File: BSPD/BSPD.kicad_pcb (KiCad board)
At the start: 2 copper layers, 9 parts, among them J1 350826-1, J2 440054-2, U1 LM339DR, U2 R-78E5.0-0.5, U3 SN74LVC1G3208DBVT, U4 SN74LVC3G14DCUR, U5 NE555DR, U6 SN74LVC1G08DBVR, U7 SN74AC32DR

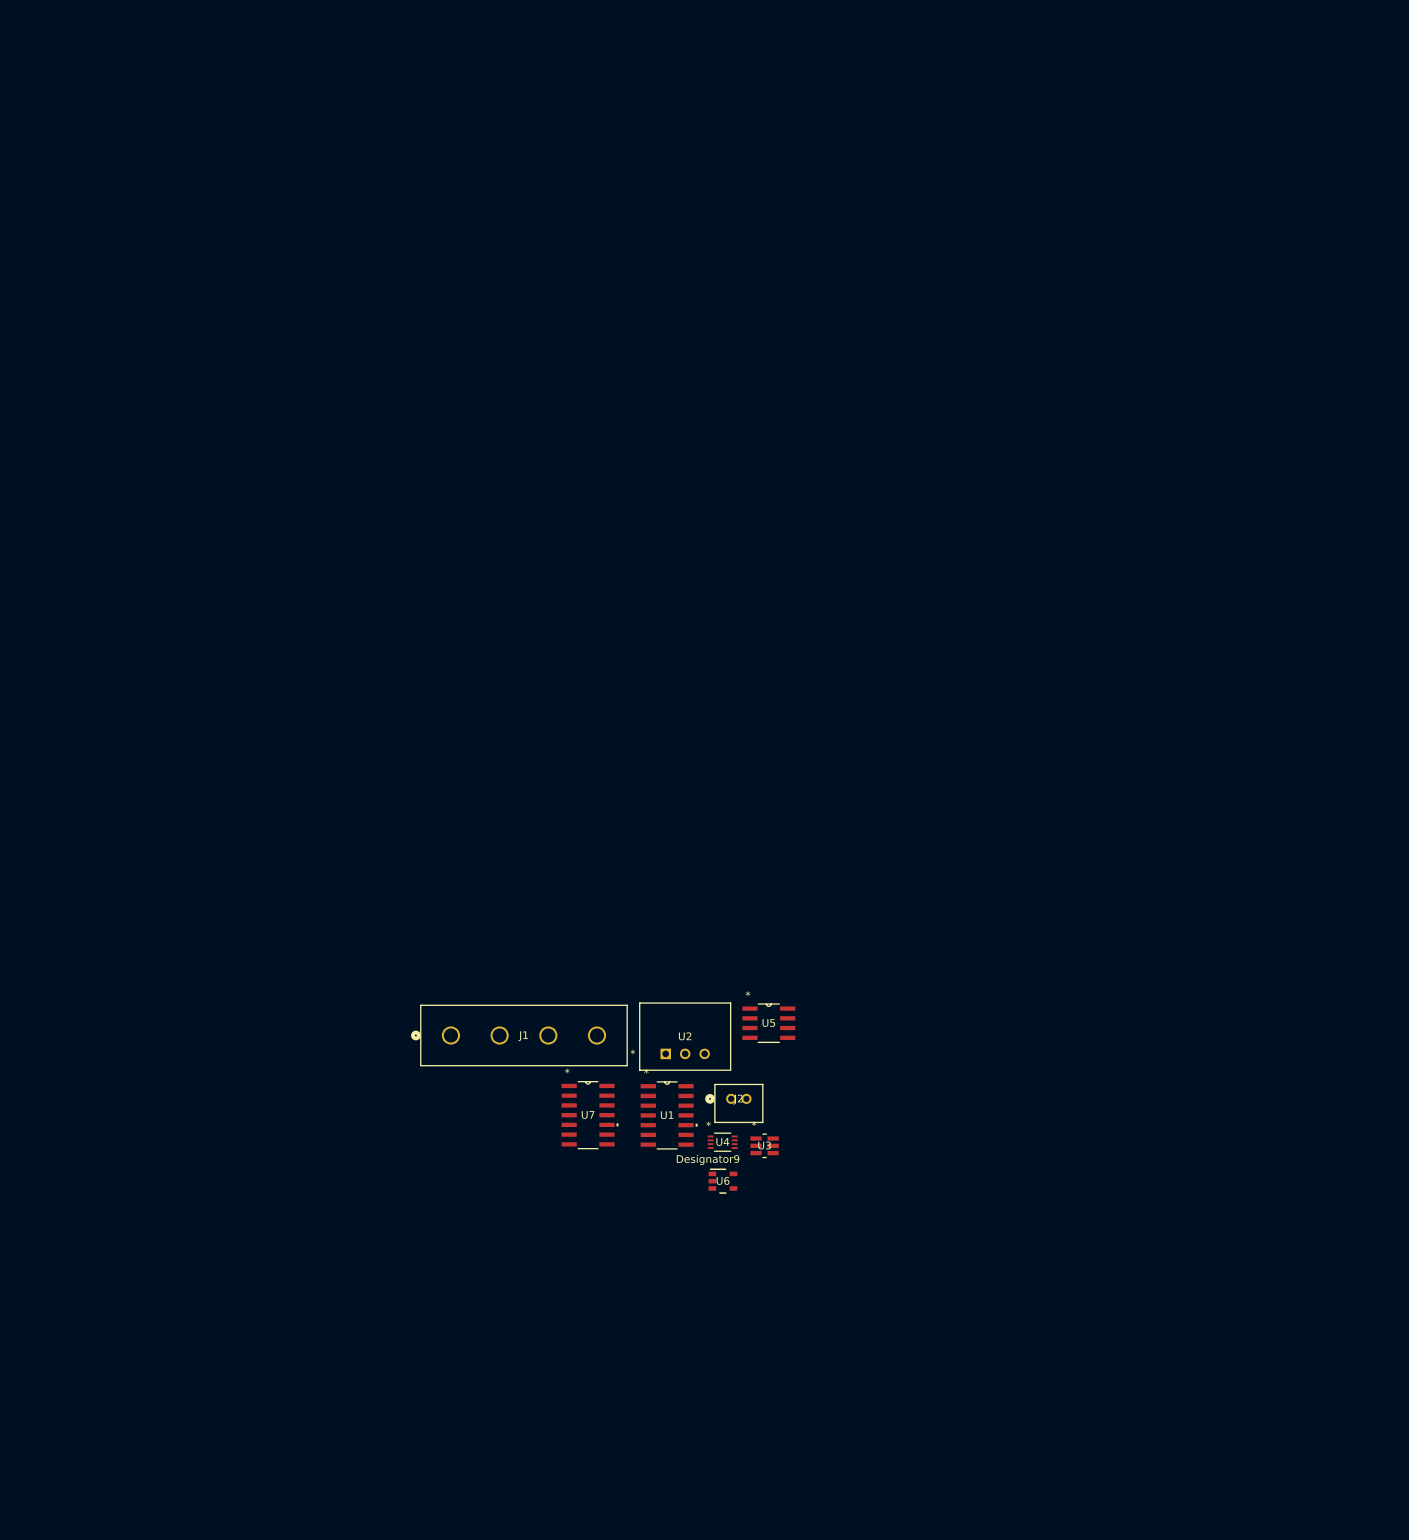
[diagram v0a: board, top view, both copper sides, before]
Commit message: Added footprints,implemented changes from meeting, starting layout
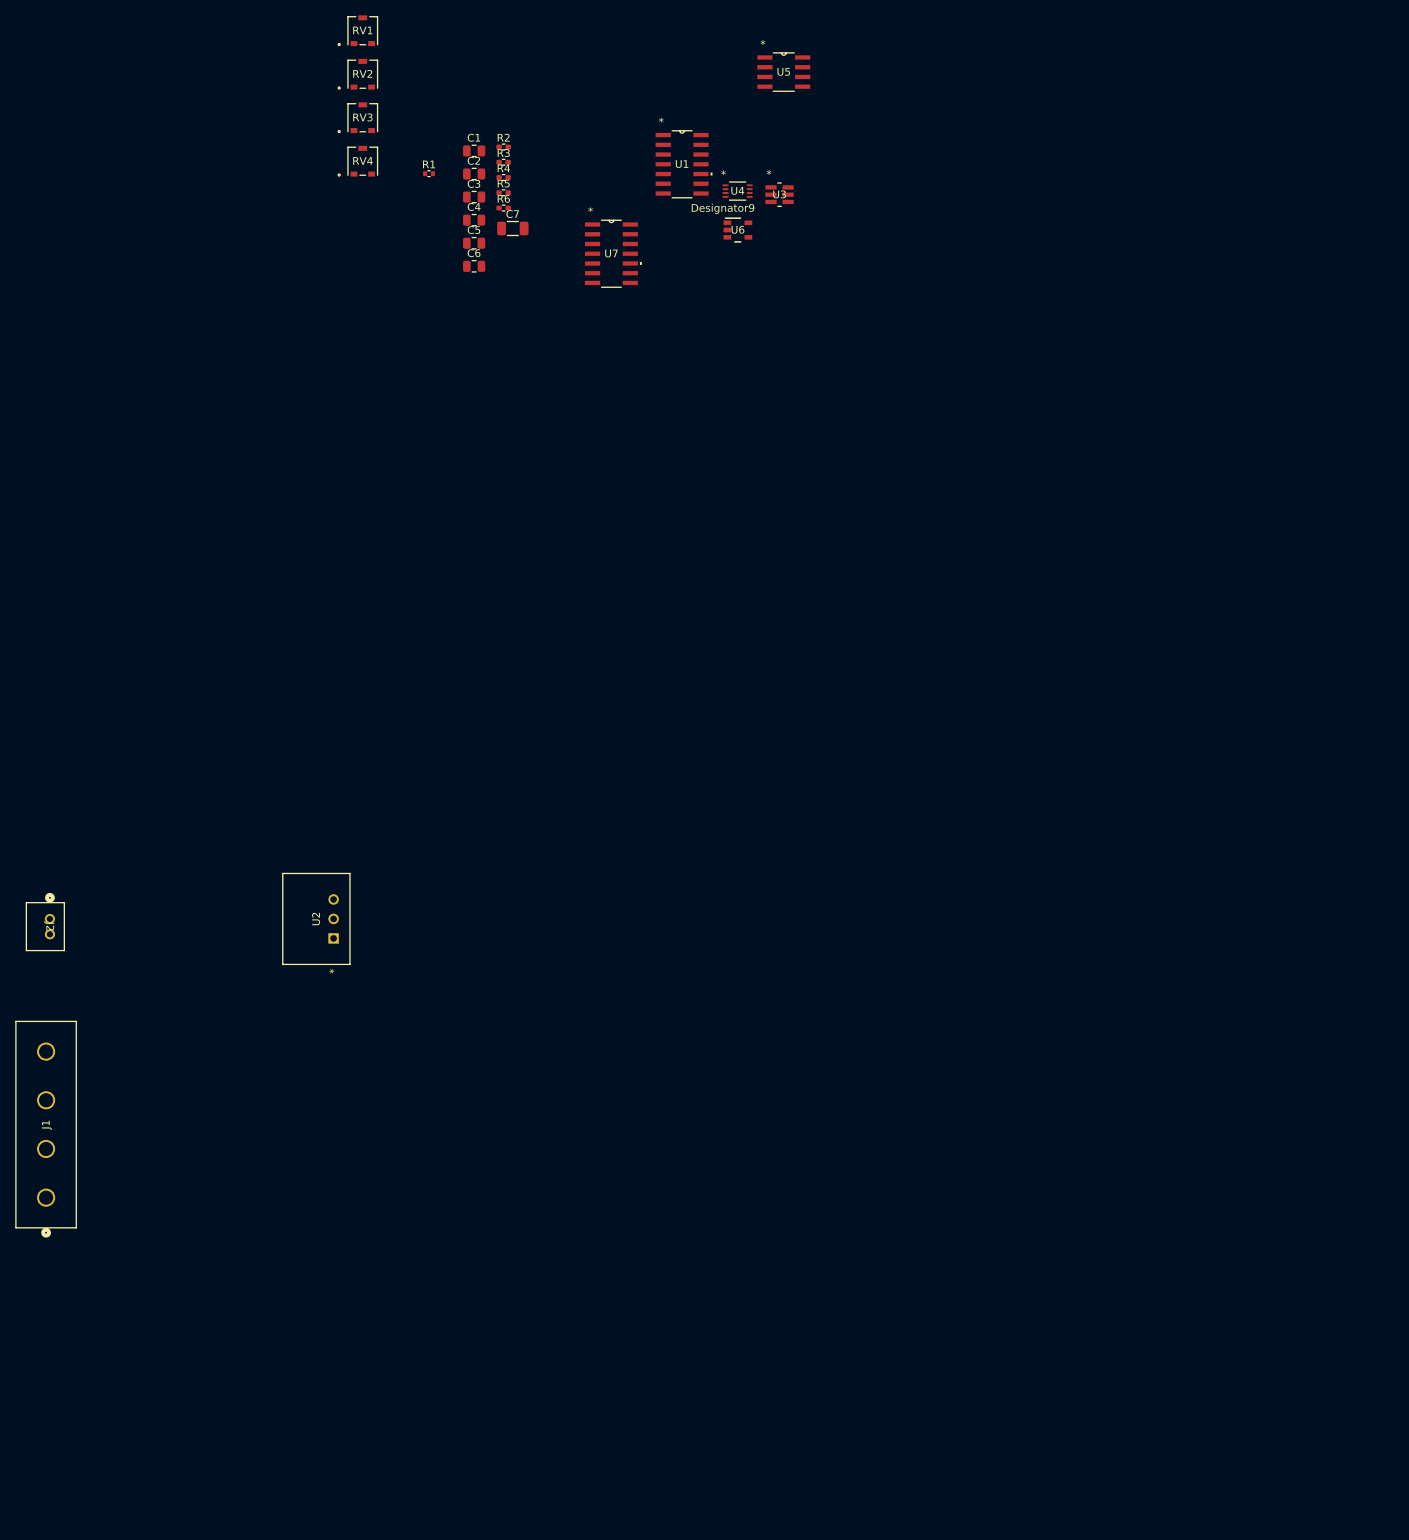
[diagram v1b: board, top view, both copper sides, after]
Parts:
- added C1: 10uF, Capacitor_SMD:C_0805_2012Metric, F.Cu at (118.3, -30.2)
- added C2: 10uF, Capacitor_SMD:C_0805_2012Metric, F.Cu at (118.3, -27.2)
- added C3: 0.1uF, Capacitor_SMD:C_0805_2012Metric, F.Cu at (118.3, -24.1)
- added C4: 10uF, Capacitor_SMD:C_0805_2012Metric, F.Cu at (118.3, -21.1)
- added C5: 0.01uF, Capacitor_SMD:C_0805_2012Metric, F.Cu at (118.3, -18.1)
- added C6: 0.1uF, Capacitor_SMD:C_0805_2012Metric, F.Cu at (118.3, -15.1)
- added C7: 100uF, Capacitor_SMD:C_1206_3216Metric, F.Cu at (123.4, -20.1)
- added R1: R_US, Resistor_SMD:R_0402_1005Metric, F.Cu at (112.4, -27.2)
- added R2: 10k, Resistor_SMD:R_0402_1005Metric_Pad0.72x0.64mm_HandSolder, F.Cu at (122.2, -30.7)
- added R3: 10K, Resistor_SMD:R_0402_1005Metric_Pad0.72x0.64mm_HandSolder, F.Cu at (122.2, -28.7)
- added R4: 10K, Resistor_SMD:R_0402_1005Metric_Pad0.72x0.64mm_HandSolder, F.Cu at (122.2, -26.7)
- added R5: 10K, Resistor_SMD:R_0402_1005Metric_Pad0.72x0.64mm_HandSolder, F.Cu at (122.2, -24.7)
- added R6: 10K, Resistor_SMD:R_0402_1005Metric_Pad0.72x0.64mm_HandSolder, F.Cu at (122.2, -22.7)
- added RV1: 10K, PVG3A103C01R00:RES_C01R00, F.Cu at (103.8, -45.8)
- added RV2: 10K, PVG3A103C01R00:RES_C01R00, F.Cu at (103.8, -40.2)
- added RV3: 10K, PVG3A103C01R00:RES_C01R00, F.Cu at (103.8, -34.5)
- added RV4: 10K, PVG3A103C01R00:RES_C01R00, F.Cu at (103.8, -28.8)
- U7: value SN74AC32DR -> SN74HC32DR; footprint LM339DR:D14 -> SN74AC32DR:D14
- moved U1 124.1 mm to (145.5, -28.4)
- moved U4 124.1 mm to (152.7, -24.9)
- moved U3 124.1 mm to (158.2, -24.5)
- moved U6 124.1 mm to (152.7, -19.8)
- moved U5 124.1 mm to (158.7, -40.5)
- moved U7 112.4 mm to (136.2, -16.8)
- moved J2 91.9 mm to (63.0, 70.0), turned to -90 degrees
- moved J1 56.9 mm to (62.5, 106.3), turned to 90 degrees
- moved U2 45.9 mm to (100.0, 72.5), turned to 90 degrees
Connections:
- U1 pad 10: 4IN- -> HARD_BREAK
- U1 pad 5: 2IN+ -> THRESH_THROTTLE
- U1 pad 7: 1IN+ -> THRESH_BSE
- U1 pad 8: 3IN- -> 10%_THROTTLE
- U7 pad 11: Net-(U7-3B) -> unconnected-(U7-4Y-Pad11)
- U7 pad 12: Net-(U1-OUT3) -> Net-(U7-4A)
- U7 pad 13: Net-(U1-OUT4) -> Net-(U7-4A)
- U7 pad 14: Net-(U7-VCC) -> Net-(U7-4A)
- U7 pad 4: unconnected-(U7-2A-Pad4) -> Net-(U7-2A)
- U7 pad 5: unconnected-(U7-2B-Pad5) -> Net-(U7-2A)
- U7 pad 8: unconnected-(U7-3Y-Pad8) -> BSPD_OUT

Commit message: Updating footprints
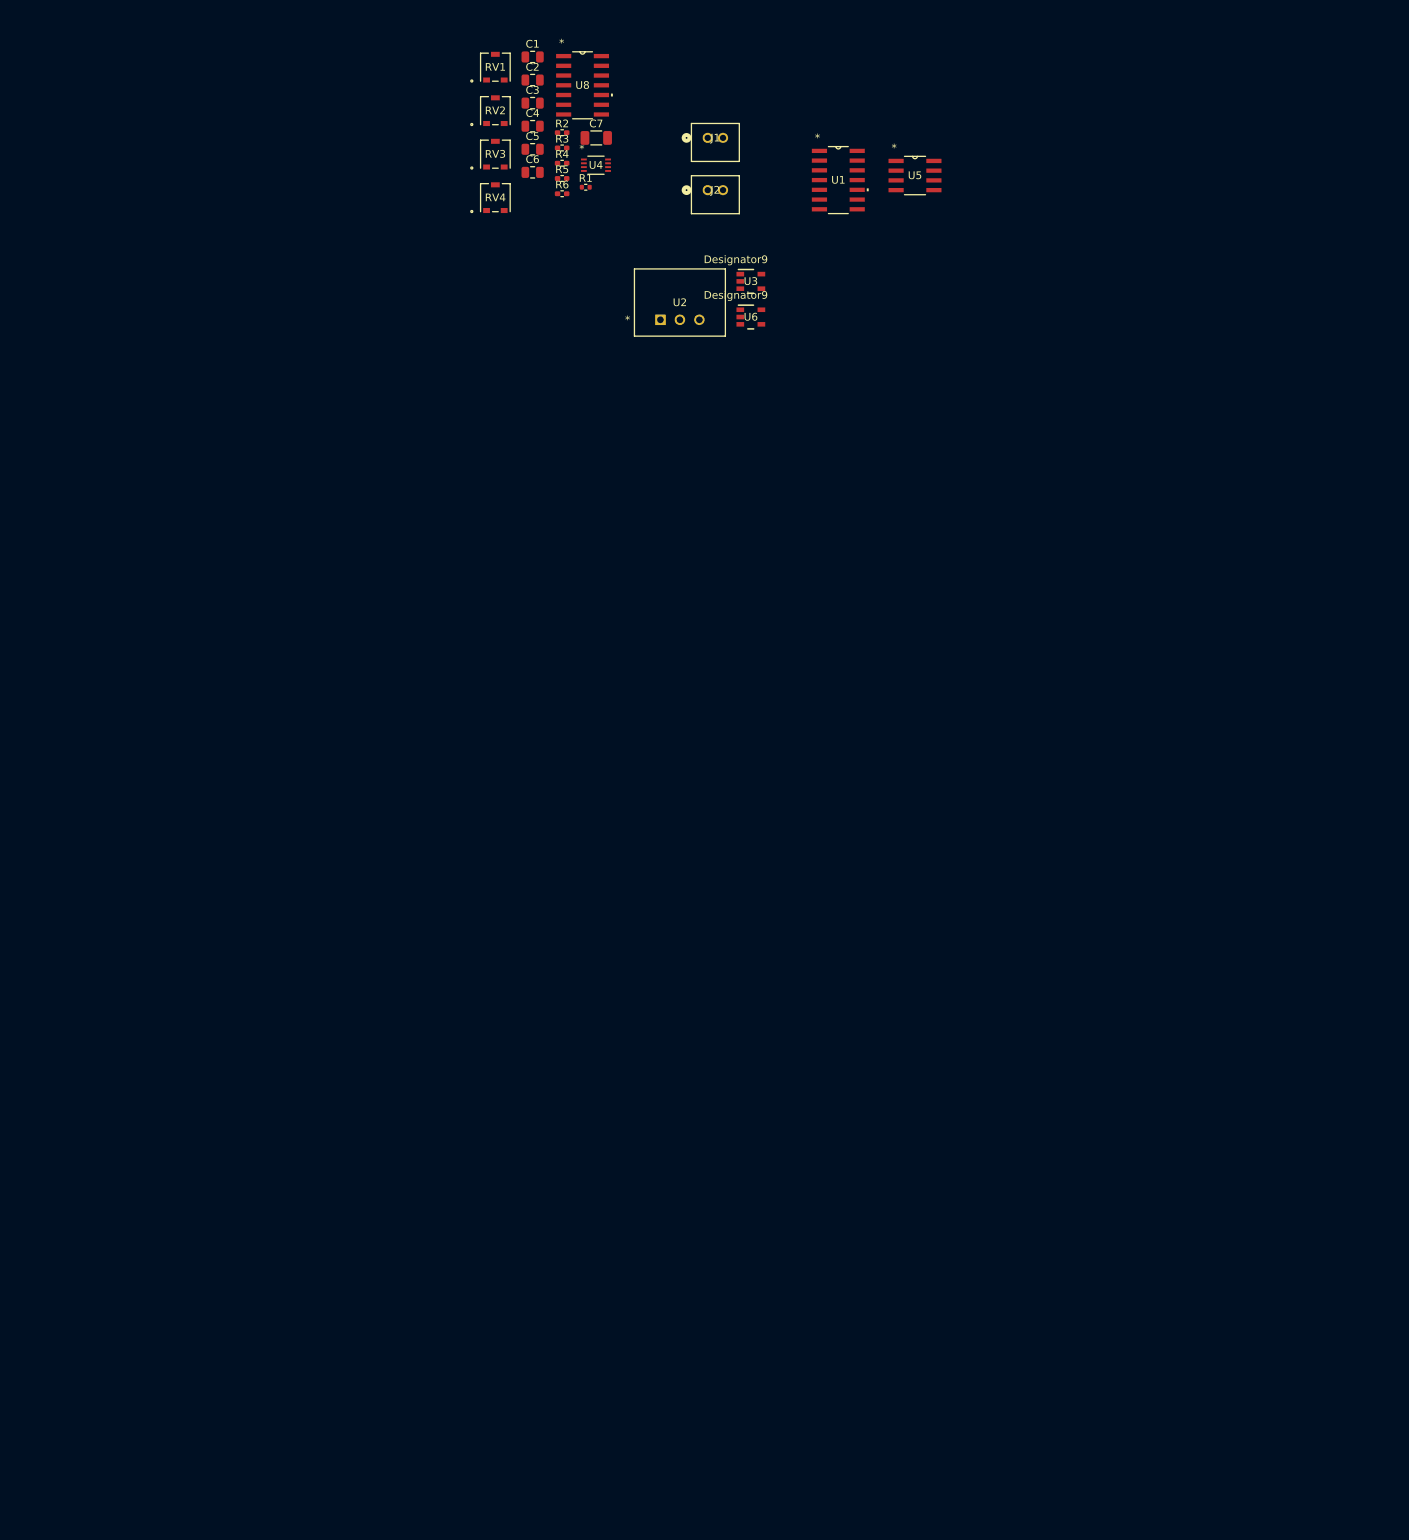
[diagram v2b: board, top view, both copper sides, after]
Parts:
- removed U7: SN74HC32DR, SN74AC32DR:D14
- added U8: SN74AC32DR, LM339DR:D14, F.Cu at (132.5, -38.7)
- J1: value 350826-1 -> 440054-2; footprint 350826-1:CONN_350826-1_TYC -> 440054_2:CONN2_440054-2_TYC
- U3: value SN74LVC1G3208DBVT -> SN74LVC1G08DBVR; footprint SN74LVC1G3208DBVT:DBV6 -> SN74LVC1G08DBVR:DBV0005A_N
- moved J1 162.9 mm to (148.8, -31.9), turned to 0 degrees
- moved J2 128.0 mm to (148.8, -25.1), turned to 0 degrees
- moved U2 91.3 mm to (142.6, -8.15), turned to 0 degrees
- moved U5 21.8 mm to (175.8, -27.0)
- moved R1 20.5 mm to (132.9, -25.4)
- moved U1 20.5 mm to (165.8, -26.4)
- moved U4 18.8 mm to (134.2, -28.3)
- moved RV1 17.9 mm to (121.1, -41.1)
- moved RV2 17.9 mm to (121.1, -35.4)
- moved RV3 17.9 mm to (121.1, -29.7)
- moved RV4 17.9 mm to (121.1, -24.1)
- moved C7 16.1 mm to (134.3, -31.9)
- moved C3 14.4 mm to (126.0, -36.4)
- moved C2 14.4 mm to (126.0, -39.4)
- moved C5 14.4 mm to (126.0, -30.4)
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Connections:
- J1 pad 2: unconnected-(J1-Pad2) -> THROTTLE_IN
- J2 pad 1: GND -> +12V
- J2 pad 2: +12V -> GND
- U3 pad 1: 2OUT -> Net-(U1-OUT3)
- U3 pad 2: GND -> Net-(U1-OUT4)
- U3 pad 3: 1OUT -> GND
- U3 pad 5: Net-(U3-C) -> Net-(U3-V+)
